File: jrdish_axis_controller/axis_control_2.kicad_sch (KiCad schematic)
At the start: 31 parts, among them CN12 KF2EDGR-2.54-9P, CN13 KF2EDGR-2.54-6P

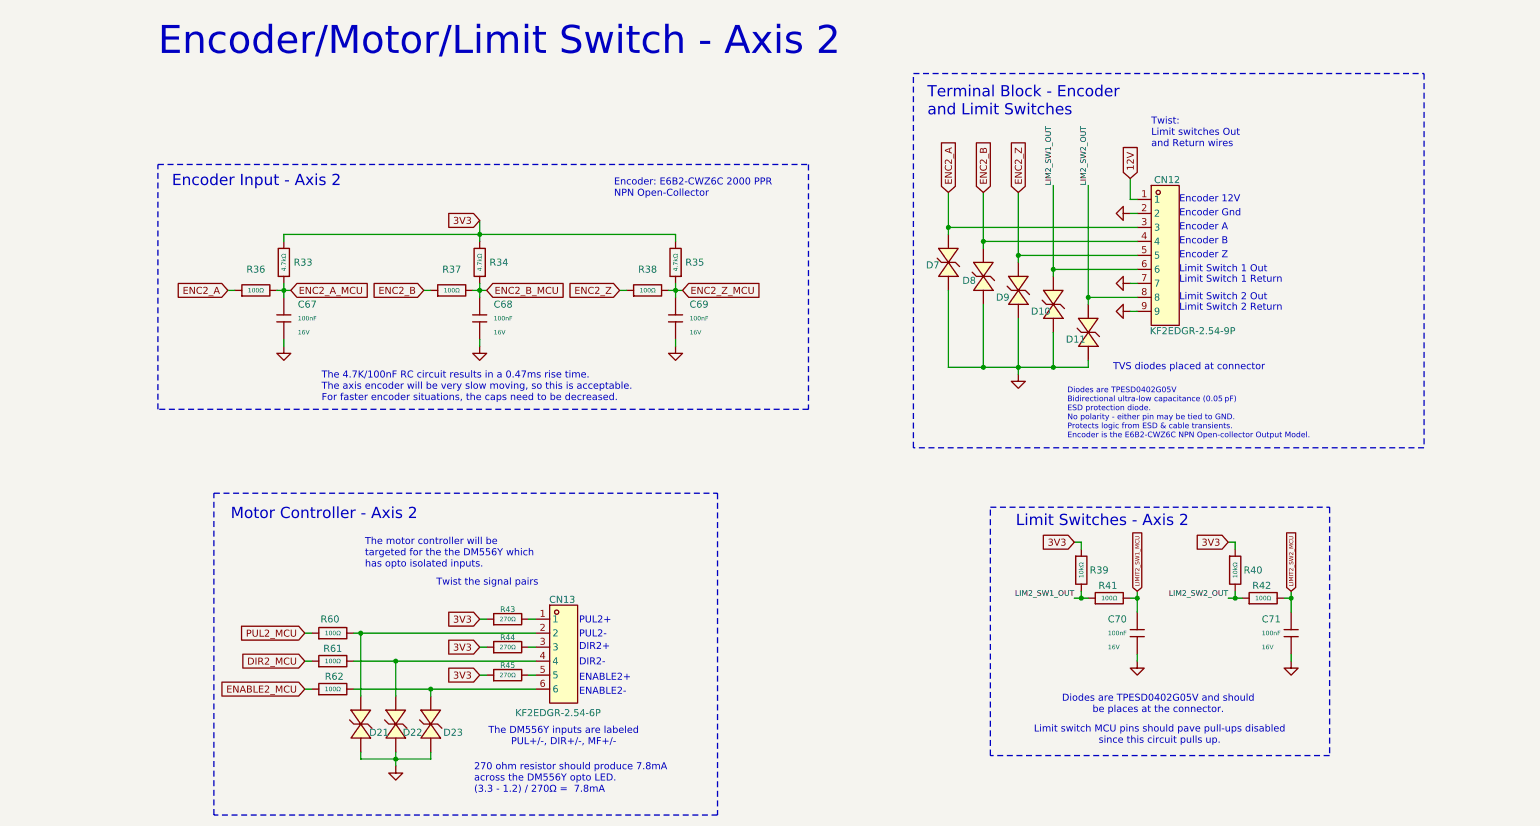
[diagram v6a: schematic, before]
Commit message: Limit switches with mosfets
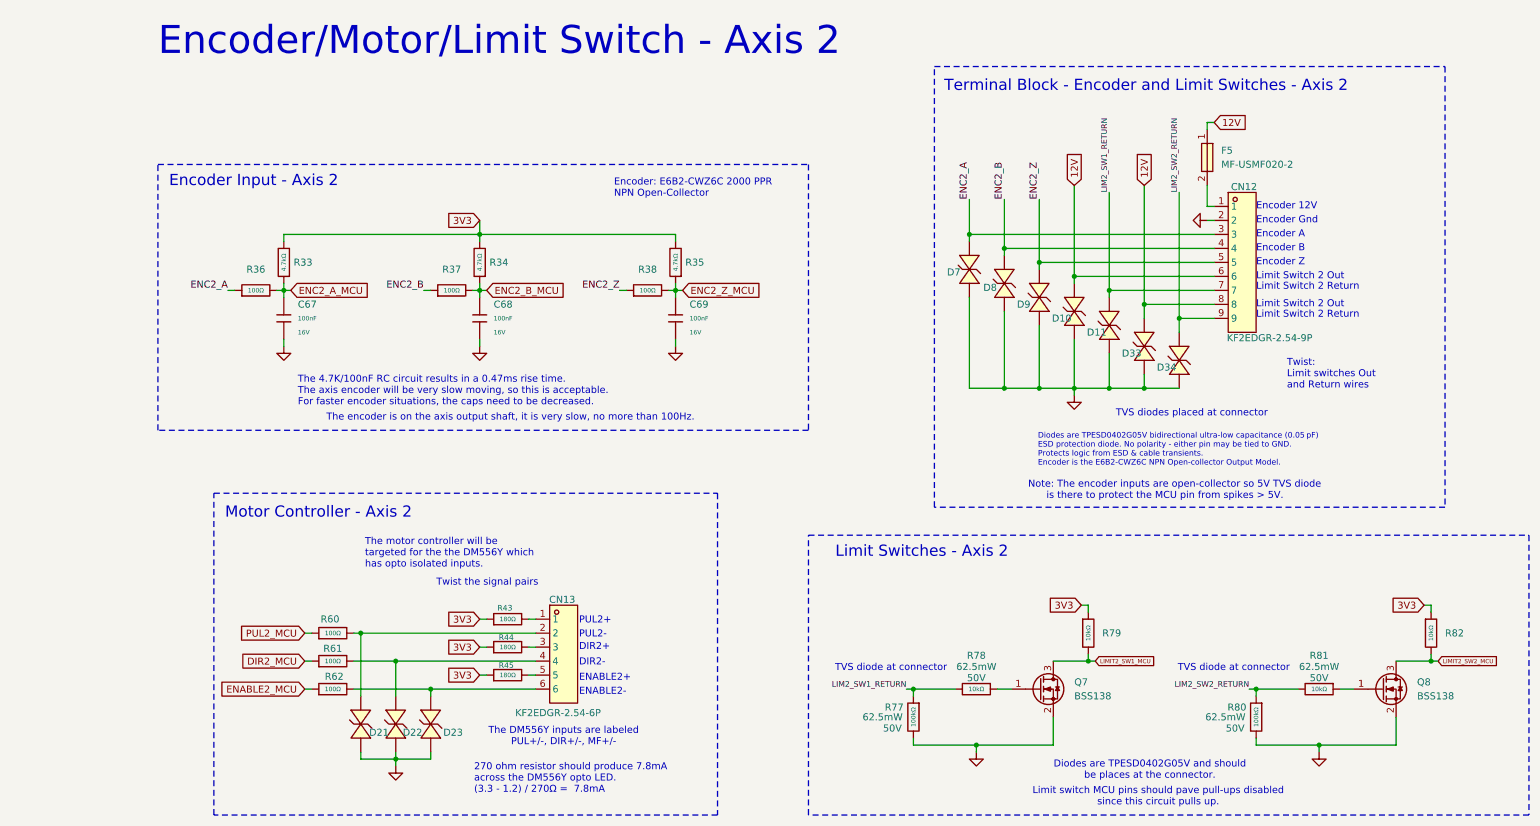
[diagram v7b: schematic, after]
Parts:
- removed C70, C71: 100nF, PCM_JLCPCB:C_0402, symbol PCM_JLCPCB-Capacitors:0402,100nF
- removed R39, R40: 10kΩ, PCM_JLCPCB:R_0402, symbol PCM_JLCPCB-Resistors:0402,10kΩ
- removed R41, R42: 100Ω, PCM_JLCPCB:R_0402, symbol PCM_JLCPCB-Resistors:0402,100Ω
- removed R43, R44, R45: 270Ω, PCM_JLCPCB:R_0603, symbol PCM_JLCPCB-Resistors:0603,270Ω
- added D33, D34: TPESD0402G05V, MyParts:D0402-BI, symbol MyParts:TPESD0402G05V
- added F5: MF-USMF020-2, MyParts:F1210, symbol MyParts:MF-USMF020-2
- added Q7, Q8: BSS138, Package_TO_SOT_SMD:SOT-23, symbol Transistor_FET:BSS138
- added R43, R44, R45: 180Ω, PCM_JLCPCB:R_0603, symbol PCM_JLCPCB-Resistors:0603,180Ω
- added R77, R80: 100kΩ, PCM_JLCPCB:R_0402, symbol PCM_JLCPCB-Resistors:0402,100kΩ
- added R78, R79, R81, R82: 10kΩ, PCM_JLCPCB:R_0402, symbol PCM_JLCPCB-Resistors:0402,10kΩ
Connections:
- net LIM2_SW1_OUT is gone; now on net 12V: CN12.6, D10.1 (K)
- net 12V: now also CN12.8, D33.1 (K), F5.1; no longer CN12.1
- net 3V3: now also R43.1, R44.1, R45.1, R79.1, R82.1
- net LIMIT2_SW1_MCU: now also Q7.3 (D), R79.2
- net LIMIT2_SW2_MCU: now also Q8.3 (D), R82.2
- net GND: now reaches C68.2
- net GND: now also C67.2, C69.2, CN12.2, D10.2 (A), D11.2 (A), D21.2 (A), D22.2 (A), D23.2 (A), D7.2 (A), D8.2 (A), D9.2 (A), D33.2 (A), D34.2 (A), Q7.2 (S), Q8.2 (S), R77.2, R80.2
- net at CN13.1: now also R43.2
- net at CN13.3: now also R44.2
- net at CN13.5: now also R45.2
- net LIM2_SW1_RETURN: now reaches CN12.7
- net LIM2_SW1_RETURN: now also D11.1 (K), R77.1, R78.2
- net LIM2_SW2_RETURN: now reaches CN12.9
- net LIM2_SW2_RETURN: now also D34.1 (K), R80.1, R81.2
- removed net LIM2_SW2_OUT: CN12.8, D11.1 (K)
- new net: Q8.1 (G), R81.1
- new net: Q7.1 (G), R78.1
- new net: CN12.1, F5.2
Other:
- note added: "Diodes are TPESD0402G05V bidirectional ultra-low capacitance (0.05 pF) ESD protection diode. No polarity - either pin may be tied to GND. Protects logic from ESD & cable transients. Encoder is the E6B2-CWZ6C NPN Open-collector Output Model."
- note added: "Note: The encoder inputs are open-collector so 5V TVS diode is there to protect the MCU pin from spikes > 5V."
- note added: "TVS diode at connector"
- note added: "Terminal Block - Encoder and Limit Switches - Axis 2"
- note added: "The encoder is on the axis output shaft, it is very slow, no more than 100Hz."
- note removed: "Diodes are TPESD0402G05V Bidirectional ultra-low capacitance (0.05 pF) ESD protection diode. No polarity - either pin may be tied to GND. Protects logic from ESD & cable transients. Encoder is the E6B2-CWZ6C NPN Open-collector Output Model."
- note removed: "Limit Switch 1 Out"
- note removed: "Limit Switch 1 Return"
- note removed: "Terminal Block - Encoder and Limit Switches"

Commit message: Refinements...
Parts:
- removed D10, D11, D33, D34: TPESD0402G05V, MyParts:D0402-BI, symbol MyParts:TPESD0402G05V
- added D10, D11, D33, D34: TPESD0402G15V, MyParts:D0402-BI, symbol MyParts:TPESD0402G15V
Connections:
- net 12V: now also D10.2, D33.2
- net GND: now also D10.1, D11.1, D33.1, D34.1
- net LIM2_SW1_RETURN: now also D11.2
- net LIM2_SW2_RETURN: now also D34.2
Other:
- note added: "Diodes are TPESD0402G05V and TPESD0402G05V bidirectional ultra-low capacitance (0.05 pF) ESD protection diode. No polarity - either pin may be tied to GND. Protects logic from ESD & cable transients. Encoder is the E6B2-CWZ6C NPN Open-collector Output Model."
- note added: "Diodes are TPESD0402G05V and should be placed at the connector."
- note removed: "Diodes are TPESD0402G05V and should be places at the connector."
- note removed: "Diodes are TPESD0402G05V bidirectional ultra-low capacitance (0.05 pF) ESD protection diode. No polarity - either pin may be tied to GND. Protects logic from ESD & cable transients. Encoder is the E6B2-CWZ6C NPN Open-collector Output Model."
